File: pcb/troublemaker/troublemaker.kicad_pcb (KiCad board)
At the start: 2 copper layers, 17.8 x 40.6 mm, 114 parts, among them IC1 TEENSY_4.1, J1 neopixel_data_RPI19_GPIO10, J3 5V_RPI2_OR_4, J4 GND_RPI34, J5 Conn_01x12, SW1 sw_eq2, SW10 sw_grain_playback, SW11 btn_sampler_stop, SW2 sw_eq1, SW3 sw_sub, SW4 sw_bass, SW5 sw_mid, SW6 sw_high, SW7 btn_delay_taptempo, SW8 sw_delay_type, SW9 sw_grain_type, U1 RASPBERRY_PI_4B_4GB, U2 CD74HC4067M, U3 CD74HC4067M, U4 CD74HC4067M, U5 CD74HC4067M, U6 CD74HC4067M

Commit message: Fixed some issues with the PCB
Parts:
- moved RV76 512.8 mm to (99.1, 391.1)
- moved RV17 509.6 mm to (53.5, 387.1)
- moved RV16 506.2 mm to (53.5, 353.1)
- moved RV15 503.4 mm to (53.5, 319.1)
- moved RV14 501.3 mm to (53.5, 285.1)
- moved RV13 499.9 mm to (53.5, 251.2)
- moved RV12 499.2 mm to (53.5, 216.2)
- moved RV77 492.8 mm to (137.0, 391.2)
- moved RV67 482.7 mm to (147.0, 350.1)
- moved RV22 479.1 mm to (102.5, 353.1)
- moved RV21 476.2 mm to (102.5, 319.2)
- moved RV20 474.0 mm to (102.5, 285.1)
- moved RV19 472.4 mm to (102.5, 251.2)
- moved RV18 471.6 mm to (102.5, 216.2)
- moved RV78 468.9 mm to (178.0, 391.2)
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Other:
- board size 17.8 x 40.6 mm -> 419 x 394 mm

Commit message: Fixed IC footprints having edge cuts
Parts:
- moved J1 326.9 mm to (97.6, 326.4)
- moved J3 326.9 mm to (77.6, 326.7)
- moved J4 326.9 mm to (115.6, 326.7)
- moved U1 326.9 mm to (108.9, 357.7)
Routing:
- net 3v3: track 0.00 -> 31.3 mm
- net GND: track 0.00 -> 4.30 mm
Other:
- board text added: "USB C POWER THIS SIDE"

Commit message: JLCPCB DRC, pots are connected to muxers, rearranged scheme, added missing LED resistor and pin header
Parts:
- added J2: taptempo_led_RPI16_GPIO23, Connector_PinHeader_1.00mm:PinHeader_1x01_P1.00mm_Vertical, B.Cu at (174.6, 250.0)
- added R1: R 75ohm, Resistor_THT:R_Axial_DIN0207_L6.3mm_D2.5mm_P10.16mm_Horizontal, F.Cu at (158.8, 240.1)
- C1, C2, C3, C4, C5, IC1, J1, J3, J4, J5, U1, U2, U3, U4, U5, U6: moved to B.Cu
- taptempo_led1: value LED -> LED chartreuse 1.8-2V, 20mA
- moved U2 306.0 mm to (360.7, 63.9), turned to 90 degrees
- moved C1 298.5 mm to (353.9, 52.3), turned to 180 degrees
- moved U5 227.2 mm to (83.2, 298.1), turned to 0 degrees
- moved C4 222.6 mm to (94.4, 291.2), turned to 90 degrees
- moved RV31 164.7 mm to (307.7, 102.2)
- moved RV32 164.7 mm to (327.7, 129.2)
- moved RV33 164.7 mm to (307.7, 156.2)
- moved RV34 164.7 mm to (323.7, 187.2)
- moved J5 155.3 mm to (202.6, 89.4), turned to 90 degrees
- moved U1 128.8 mm to (143.8, 233.7), turned to 90 degrees
- moved J4 117.1 mm to (174.3, 225.3), turned to 90 degrees
- moved J3 114.5 mm to (174.3, 265.3), turned to 90 degrees
- moved U4 112.4 mm to (299.1, 266.9), turned to 90 degrees
- moved J1 112.1 mm to (174.6, 244.9), turned to 90 degrees
- moved U3 102.8 mm to (247.3, 156.4), turned to 90 degrees
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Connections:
- RV12 pad 2: Net-(U2-I11) -> Net-(U5-I0)
- RV13 pad 2: Net-(U2-I12) -> Net-(U5-I2)
- RV14 pad 2: Net-(U2-I13) -> Net-(U5-I4)
- RV15 pad 2: Net-(U2-I14) -> Net-(U5-I6)
- RV16 pad 2: Net-(U2-I15) -> Net-(U5-I8)
- RV17 pad 2: Net-(U3-I0) -> Net-(U5-I10)
- RV18 pad 2: Net-(U3-I1) -> Net-(U5-I1)
- RV19 pad 2: Net-(U3-I2) -> Net-(U5-I3)
- RV20 pad 2: Net-(U3-I3) -> Net-(U5-I5)
- RV21 pad 2: Net-(U3-I4) -> Net-(U5-I7)
- RV22 pad 2: Net-(U3-I5) -> Net-(U5-I9)
- RV23 pad 2: Net-(U3-I6) -> Net-(U2-I11)
- RV24 pad 2: Net-(U3-I7) -> Net-(U2-I12)
- RV25 pad 2: unconnected-(RV25-Pad2) -> Net-(U2-I13)
- RV26 pad 2: unconnected-(RV26-Pad2) -> Net-(U2-I14)
- RV27 pad 2: Net-(U3-I10) -> Net-(U2-I15)
- RV28 pad 2: Net-(U3-I11) -> Net-(U3-I0)
- RV29 pad 2: Net-(U3-I12) -> Net-(U3-I1)
- RV30 pad 2: Net-(U3-I13) -> Net-(U3-I2)
- RV31 pad 2: Net-(U3-I14) -> Net-(U3-I3)
- RV32 pad 2: Net-(U3-I15) -> Net-(U3-I4)
- RV33 pad 2: Net-(U4-I0) -> Net-(U3-I5)
- RV34 pad 2: Net-(U4-I1) -> Net-(U3-I6)
- RV35 pad 2: Net-(U4-I2) -> Net-(U3-I7)
- RV36 pad 2: Net-(U4-I3) -> Net-(U3-I8)
- RV37 pad 2: Net-(U4-I4) -> Net-(U3-I9)
- RV38 pad 2: Net-(U4-I5) -> Net-(U3-I10)
- RV39 pad 2: Net-(U4-I7) -> Net-(U3-I12)
- RV47 pad 2: Net-(U4-I6) -> Net-(U3-I11)
- RV48 pad 2: Net-(U4-I8) -> Net-(U3-I13)
- RV49 pad 2: Net-(U4-I9) -> Net-(U3-I14)
- RV50 pad 2: Net-(U4-I10) -> Net-(U3-I15)
- RV51 pad 2: Net-(U4-I11) -> Net-(U4-I0)
- RV52 pad 2: Net-(U4-I12) -> Net-(U4-I1)
- RV53 pad 2: Net-(U4-I13) -> Net-(U4-I2)
- RV54 pad 2: Net-(U4-I14) -> Net-(U4-I3)
- RV55 pad 2: Net-(U4-I15) -> Net-(U4-I4)
- RV56 pad 2: Net-(U5-I0) -> Net-(U4-I5)
- RV57 pad 2: Net-(U5-I1) -> Net-(U4-I6)
- RV58 pad 2: Net-(U5-I2) -> Net-(U4-I7)
- RV59 pad 2: Net-(U5-I3) -> Net-(U4-I8)
- RV60 pad 2: Net-(U5-I4) -> Net-(U4-I9)
- RV61 pad 2: Net-(U5-I5) -> Net-(U4-I10)
- RV62 pad 2: Net-(U5-I6) -> Net-(U4-I11)
- RV63 pad 2: Net-(U5-I7) -> Net-(U4-I12)
- RV64 pad 2: Net-(U5-I8) -> Net-(U4-I13)
- RV65 pad 2: Net-(U5-I9) -> Net-(U4-I14)
- RV66 pad 2: Net-(U5-I10) -> Net-(U4-I15)
- RV70 pad 2: Net-(U5-I14) -> Net-(U6-I0)
- RV71 pad 2: Net-(U5-I15) -> Net-(U6-I1)
- RV72 pad 2: Net-(U6-I0) -> Net-(U6-I2)
- RV73 pad 2: Net-(U6-I1) -> Net-(U6-I3)
- RV74 pad 2: Net-(U6-I2) -> Net-(U6-I4)
- RV75 pad 2: Net-(U6-I3) -> Net-(U6-I5)
- RV76 pad 2: Net-(U6-I4) -> Net-(U6-I6)
- RV77 pad 2: Net-(U6-I5) -> Net-(U6-I7)
- RV78 pad 2: Net-(U6-I6) -> Net-(U6-I8)
- RV79 pad 2: Net-(U6-I7) -> Net-(U6-I9)
- RV80 pad 2: Net-(U6-I8) -> Net-(U6-I10)
- RV81 pad 2: Net-(U6-I9) -> Net-(U6-I11)
- RV82 pad 2: Net-(U6-I10) -> Net-(U6-I12)
- RV83 pad 2: Net-(U6-I11) -> Net-(U6-I13)
- RV84 pad 2: Net-(U6-I12) -> Net-(U6-I14)
- RV85 pad 2: Net-(U6-I13) -> Net-(U6-I15)
- U1 pad 16: taptempo_LED -> unconnected-(U1-GPIO23/GPIO_GEN4-Pad16)
- U3 pad 22: 3v3 -> Net-(U3-I9)
- U3 pad 23: 3v3 -> Net-(U3-I8)
- U5 pad 16: Net-(U5-I15) -> unconnected-(U5-I15-Pad16)
- U5 pad 17: Net-(U5-I14) -> unconnected-(U5-I14-Pad17)
- U6 pad 16: unconnected-(U6-I15-Pad16) -> Net-(U6-I15)
- U6 pad 17: unconnected-(U6-I14-Pad17) -> Net-(U6-I14)
- taptempo_led1 pad 2: taptempo_LED -> Net-(taptempo_led1-A)
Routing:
- net Net-(U2-I7): track 0.00 -> 376.4 mm
- net Net-(U2-I10): track 0.00 -> 336.2 mm
- net Net-(U2-I6): track 0.00 -> 331.5 mm
- net Net-(U2-I5): track 0.00 -> 328.5 mm
- net Net-(U2-I14): track 0.00 -> 315.0 mm
- net Net-(U2-I13): track 0.00 -> 298.6 mm
- net Net-(U2-I9): track 0.00 -> 288.5 mm
- net Net-(U2-I8): track 0.00 -> 287.1 mm
- net Net-(U2-I12): track 0.00 -> 253.5 mm
- net Net-(U2-I11): track 0.00 -> 244.3 mm
- net Net-(U6-I6): track 0.00 -> 229.0 mm
- net Net-(U3-I11): track 0.00 -> 204.9 mm, vias 0 -> 2
- net Net-(U5-I13): track 0.00 -> 198.0 mm
- net Net-(U6-I7): track 0.00 -> 193.3 mm
- net Net-(U3-I7): track 0.00 -> 190.0 mm
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
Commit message: GND + 3v3 connections
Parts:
- moved C5 137.0 mm to (240.5, 145.2), turned to 180 degrees
- moved C3 54.0 mm to (292.1, 255.3)
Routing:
- net GND: track 41.7 -> 3849.7 mm, vias 0 -> 4
- net 3v3: track 9.42 -> 3809.7 mm, vias 0 -> 10
- net Net-(U6-I9): track 121.3 -> 128.5 mm
- net Net-(U6-I10): track 88.1 -> 95.3 mm
- net Net-(U6-I8): track 154.9 -> 161.7 mm
- net Net-(U5-I6): track 47.3 -> 45.3 mm

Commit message: small routing fixes, saved project file after changing lib paths
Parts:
- C1, C2, C3, C4, C5: footprint Capacitor_THT:CP_Radial_D5.0mm_P2.00mm -> Library:CP_Radial_D5.0mm_P2.00mm
- IC1: footprint TEENSY_4.1:TEENSY41 -> Library:TEENSY41
- J1, J2, J3, J4: footprint Connector_PinHeader_1.00mm:PinHeader_1x01_P1.00mm_Vertical -> Library:PinHeader_1x01_P1.00mm_Vertical
- J5: footprint Connector_PinHeader_2.00mm:PinHeader_1x12_P2.00mm_Vertical -> Library:PinHeader_1x12_P2.00mm_Vertical
- Neopixel_bass_gain_reduction1, Neopixel_bass_out_level1, Neopixel_high_gain_reduction1, Neopixel_high_out_level1, Neopixel_mid_gain_reduction1, Neopixel_mid_out_level1, Neopixel_sub_gain_reduction1, Neopixel_sub_out_level1: footprint leozorLib:Neopixel-8LED -> Library:Neopixel-8LED
- R1: footprint Resistor_THT:R_Axial_DIN0207_L6.3mm_D2.5mm_P10.16mm_Horizontal -> Library:R_Axial_DIN0207_L6.3mm_D2.5mm_P10.16mm_Horizontal
- RV1, RV10, RV11, RV12, RV13, RV14, RV15, RV16, RV17, RV18, RV19, RV2, RV20, RV21, RV22, RV23, RV24, RV25, RV26, RV27, RV28, RV29, RV3, RV30, RV31, RV32, RV33, RV34, RV35, RV36, RV37, RV38, RV39, RV4, RV47, RV48, RV49, RV5, RV50, RV51, RV52, RV53, RV54, RV55, RV56, RV57, RV58, RV59, RV6, RV60, RV61, RV62, RV63, RV64, RV65, RV66, RV67, RV68, RV69, RV7, RV70, RV71, RV72, RV73, RV74, RV75, RV76, RV77, RV78, RV79, RV8, RV80, RV81, RV82, RV83, RV84, RV85, RV9: footprint Potentiometer_THT:Potentiometer_Alps_RK09K_Single_Vertical -> Library:Potentiometer_Alps_RK09K_Single_Vertical
- SW1, SW10, SW2, SW3, SW4, SW5, SW6, SW8, SW9: footprint leozorLib:SW_SPDT_red_leozor -> Library:SW_SPDT_red_leozor
- SW11, SW7: footprint leozorLib:arcade_service_button_leozor -> Library:arcade_service_button_leozor
- U1: footprint RASPBERRY_PI_4B_4GB:MODULE_RASPBERRY_PI_4B_4GB -> Library:MODULE_RASPBERRY_PI_4B_4GB
- U2, U3, U4, U5, U6: footprint leozorLib:Breakout_HC4067_PTH_Only -> Library:Breakout_HC4067_PTH_Only
- taptempo_led1: footprint LED_THT:LED_D3.0mm -> Library:LED_D3.0mm
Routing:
- net Net-(U6-I7): track 193.3 -> 207.9 mm
- net Net-(U6-I6): track 229.0 -> 241.6 mm
- net Net-(U6-I13): track 57.4 -> 67.9 mm
- net Net-(U6-I15): track 127.5 -> 137.2 mm
- net Net-(U6-I14): track 90.8 -> 100.3 mm
- net Net-(U6-I10): track 95.3 -> 100.0 mm
- net Net-(U6-I11): track 60.6 -> 65.2 mm
- net Net-(U6-I9): track 128.5 -> 133.2 mm
- net Net-(U6-I8): track 161.7 -> 166.2 mm
- net Net-(U3-I11): track 204.9 -> 208.6 mm
- net Net-(U6-I12): track 50.8 -> 54.1 mm
- net Net-(U5-I9): track 82.5 -> 85.6 mm
- net Net-(U5-I11): track 125.7 -> 128.7 mm
- net Net-(U5-I12): track 159.8 -> 162.6 mm
- net Net-(U5-I13): track 198.0 -> 200.8 mm
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
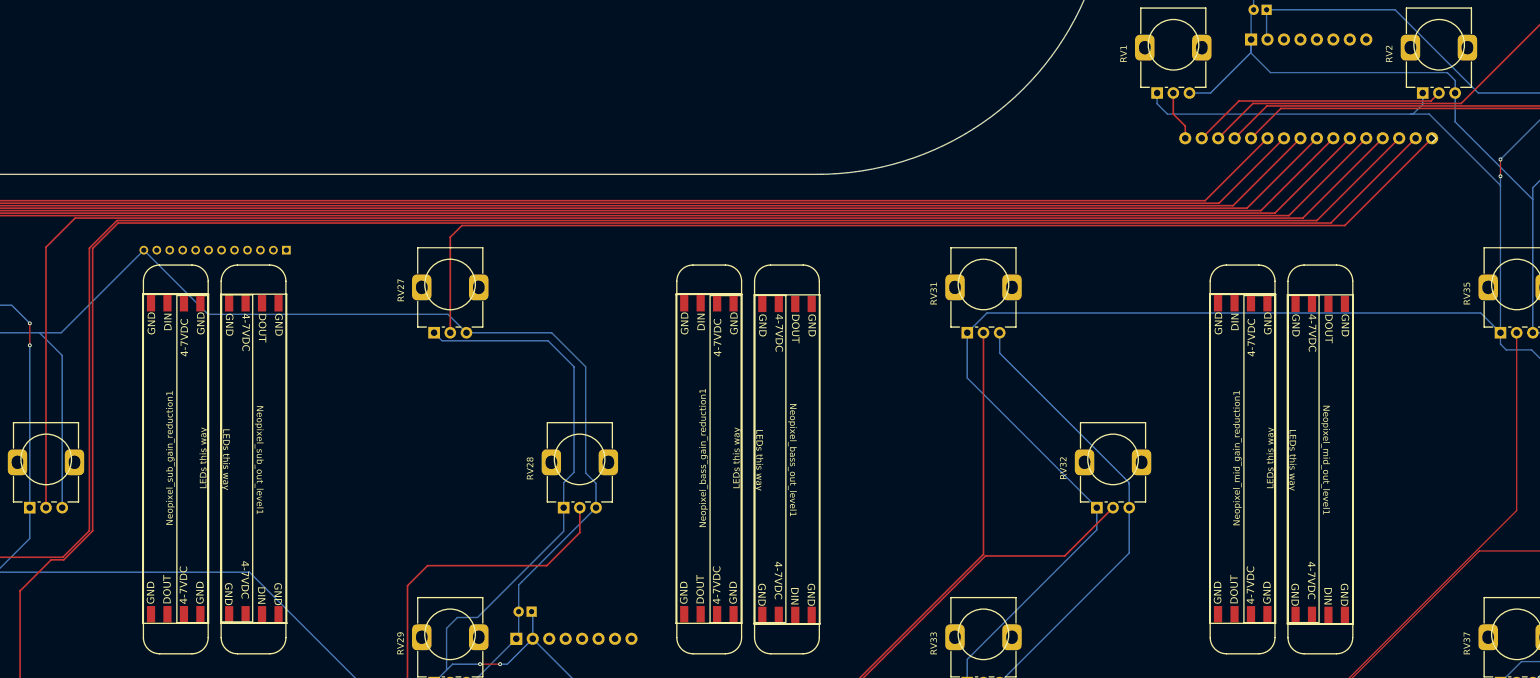
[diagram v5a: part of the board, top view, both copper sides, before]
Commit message: Working on routing the muxers
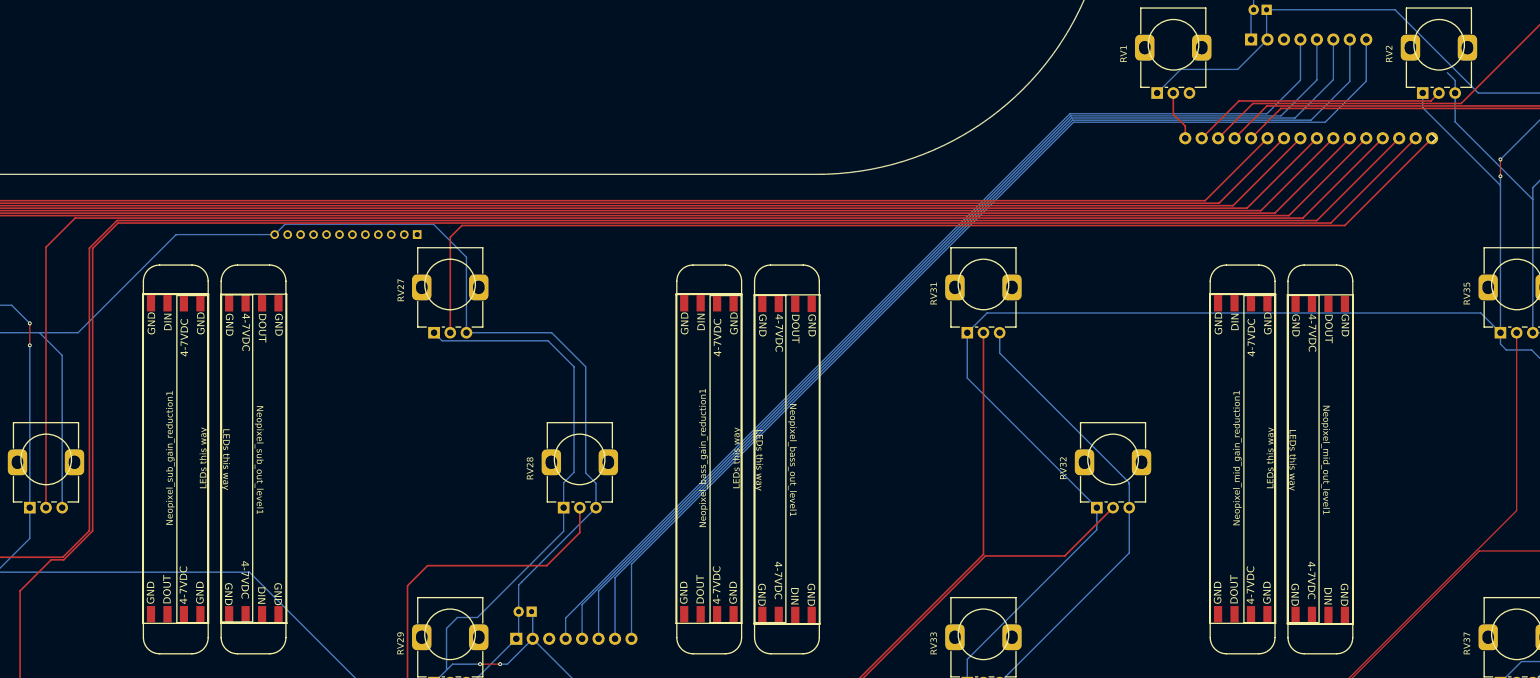
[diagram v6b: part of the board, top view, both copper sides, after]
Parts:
- moved J5 20.3 mm to (222.8, 87.0)
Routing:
- net mux_signal: track 0.00 -> 162.2 mm
- net mux_s3: track 0.00 -> 161.0 mm
- net mux_s2: track 0.00 -> 159.7 mm
- net mux_s1: track 0.00 -> 158.5 mm
- net mux_s0: track 0.00 -> 157.3 mm
- net GND: track 3850.6 -> 3813.0 mm
- net 3v3: track 3809.7 -> 3785.4 mm

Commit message: All connections done
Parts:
- C1, C2, C3, C4, C5: footprint Library:CP_Radial_D5.0mm_P2.00mm -> Capacitor_THT:CP_Radial_D5.0mm_P2.00mm
- IC1: footprint Library:TEENSY41 -> TEENSY_4.1:TEENSY41
- J1, J2, J3, J4: footprint Library:PinHeader_1x01_P1.00mm_Vertical -> Connector_PinHeader_1.00mm:PinHeader_1x01_P1.00mm_Vertical
- J5: footprint Library:PinHeader_1x12_P2.00mm_Vertical -> Connector_PinHeader_2.00mm:PinHeader_1x12_P2.00mm_Vertical
- Neopixel_bass_gain_reduction1, Neopixel_bass_out_level1, Neopixel_high_gain_reduction1, Neopixel_high_out_level1, Neopixel_mid_gain_reduction1, Neopixel_mid_out_level1, Neopixel_sub_gain_reduction1, Neopixel_sub_out_level1: footprint Library:Neopixel-8LED -> leozorLib:Neopixel-8LED
- R1: footprint Library:R_Axial_DIN0207_L6.3mm_D2.5mm_P10.16mm_Horizontal -> Resistor_THT:R_Axial_DIN0207_L6.3mm_D2.5mm_P10.16mm_Horizontal
- RV1, RV10, RV11, RV12, RV13, RV14, RV15, RV16, RV17, RV18, RV19, RV2, RV20, RV21, RV22, RV23, RV24, RV25, RV26, RV27, RV28, RV29, RV3, RV30, RV31, RV32, RV33, RV34, RV35, RV36, RV37, RV38, RV39, RV4, RV47, RV48, RV49, RV5, RV50, RV51, RV52, RV53, RV54, RV55, RV56, RV57, RV58, RV59, RV6, RV60, RV61, RV62, RV63, RV64, RV65, RV66, RV67, RV68, RV69, RV7, RV70, RV71, RV72, RV73, RV74, RV75, RV76, RV77, RV78, RV79, RV8, RV80, RV81, RV82, RV83, RV84, RV85, RV9: footprint Library:Potentiometer_Alps_RK09K_Single_Vertical -> Potentiometer_THT:Potentiometer_Alps_RK09K_Single_Vertical
- SW1, SW10, SW2, SW3, SW4, SW5, SW6, SW8, SW9: footprint Library:SW_SPDT_red_leozor -> leozorLib:SW_SPDT_red_leozor
- SW11, SW7: footprint Library:arcade_service_button_leozor -> leozorLib:arcade_service_button_leozor
- U1: footprint Library:MODULE_RASPBERRY_PI_4B_4GB -> RASPBERRY_PI_4B_4GB:MODULE_RASPBERRY_PI_4B_4GB
- U2, U3, U4, U5, U6: footprint Library:Breakout_HC4067_PTH_Only -> leozorLib:Breakout_HC4067_PTH_Only
- taptempo_led1: footprint Library:LED_D3.0mm -> LED_THT:LED_D3.0mm
- moved J1 0.25 mm to (174.6, 244.7)
- moved J3 0.25 mm to (174.3, 265.1)
- moved J4 0.25 mm to (174.3, 225.1)
- moved U1 0.25 mm to (143.8, 233.4)
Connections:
- IC1 pad 15: sw_delay_type -> sw_eq1
- IC1 pad 16: btn_delay_taptempo -> sw_eq2
- IC1 pad 17: sw_high -> sw_sub
- IC1 pad 18: sw_mid -> sw_bass
- IC1 pad 19: sw_bass -> sw_mid
- IC1 pad 20: sw_sub -> sw_high
- IC1 pad 21: sw_eq2 -> btn_delay_taptempo
- IC1 pad 22: sw_eq1 -> sw_delay_type
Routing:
- net mux_s0: track 157.3 -> 778.0 mm, vias 0 -> 12
- net mux_signal: track 162.2 -> 635.6 mm, vias 0 -> 11
- net mux_s3: track 161.0 -> 632.0 mm, vias 0 -> 12
- net mux_s1: track 158.5 -> 627.1 mm, vias 0 -> 12
- net mux_s2: track 159.7 -> 626.9 mm, vias 0 -> 12
- net sampler_stop: track 0.00 -> 404.2 mm
- net mux4_enable: track 0.00 -> 256.0 mm, vias 0 -> 2
- net sw_eq1: track 0.00 -> 232.2 mm, vias 0 -> 2
- net sw_grain_playback: track 0.00 -> 215.5 mm, vias 0 -> 7
- net sw_grain_type: track 0.00 -> 205.1 mm, vias 0 -> 7
- net mux1_enable: track 0.00 -> 199.1 mm, vias 0 -> 8
- net sw_delay_type: track 0.00 -> 191.2 mm
- net sw_eq2: track 0.00 -> 187.0 mm, vias 0 -> 2
- net +5V: track 0.00 -> 174.7 mm, vias 0 -> 3
- net mux5_enable: track 0.00 -> 170.4 mm, vias 0 -> 4
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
